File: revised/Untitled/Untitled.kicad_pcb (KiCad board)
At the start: 2 copper layers, 168 x 134.2 mm, 42 parts, among them J1 Conn_01x02_Pin, J2 USB_C_Receptacle_USB2.0_16P, J3 ARM Cortex Debug, J4 Conn_Coaxial, J5 Screw_Terminal_01x02, J6 Screw_Terminal_01x02, J7 Screw_Terminal_01x02, Q1 Q_PMOS, Q2 NMOS, Q3 NMOS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

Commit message: layout revised
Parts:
- J5, J7: footprint TerminalBlock:TerminalBlock_MaiXu_MX126-5.0-02P_1x02_P5.00mm -> TerminalBlock_Phoenix:TerminalBlock_Phoenix_MKDS-1,5-2-5.08_1x02_P5.08mm_Horizontal
- moved J7 153.1 mm to (123.7, 144.8)
- moved Q3 136.8 mm to (127.0, 135.5)
- moved R8 135.8 mm to (133.2, 134.2), turned to 90 degrees
- moved R9 134.8 mm to (131.5, 134.2), turned to 90 degrees
- moved C15 115.2 mm to (124.6, 171.0)
- moved C14 115.2 mm to (124.6, 168.5)
- moved J5 100.1 mm to (135.2, 145.2)
- moved D1 92.4 mm to (159.5, 118.9), turned to -90 degrees
- moved Q2 90.0 mm to (137.8, 137.5)
- moved R4 89.0 mm to (163.0, 120.7), turned to -90 degrees
- moved R5 88.5 mm to (166.2, 119.7)
- moved C5 86.0 mm to (159.2, 112.4), turned to 180 degrees
- moved U3 84.2 mm to (165.8, 110.2)
- moved C7 80.1 mm to (159.1, 110.2), turned to 180 degrees
- moved Q1 79.1 mm to (164.5, 116.7), turned to 180 degrees
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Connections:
- Q2 pad 1: Net-(J5-Pin_1) -> Net-(J5-Pin_2)
- Q2 pad 3: Net-(J5-Pin_2) -> Net-(J5-Pin_1)
- Q3 pad 1: Net-(J7-Pin_1) -> Net-(J7-Pin_2)
- Q3 pad 3: Net-(J7-Pin_2) -> Net-(J7-Pin_1)
- U2 pad 26: SWDIO -> RADIO_SCK
- U2 pad 27: SWCLK -> RADIO_MISO
- U2 pad 28: unconnected-(U2-PB15-Pad28) -> RADIO_MOSI
- U2 pad 34: RADIO_SCK -> SWDIO
- U2 pad 37: RADIO_MISO -> SWCLK
- U2 pad 38: RADIO_MOSI -> unconnected-(U2-PA15-Pad38)
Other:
- board size 168 x 134.2 mm -> 73.5 x 67.1 mm

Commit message: signal routing start
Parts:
- added H1: MountingHole_Pad, MountingHole:MountingHole_4.3mm_M4_DIN965_Pad_TopBottom, F.Cu at (161.5, 145.5)
- added H2: MountingHole_Pad, MountingHole:MountingHole_4.3mm_M4_DIN965_Pad_TopBottom, F.Cu at (105.0, 145.0)
- added H3: MountingHole_Pad, MountingHole:MountingHole_4.3mm_M4_DIN965_Pad_TopBottom, F.Cu at (105.0, 94.5)
- added H4: MountingHole_Pad, MountingHole:MountingHole_4.3mm_M4_DIN965_Pad_TopBottom, F.Cu at (161.5, 94.5)
- moved C1 24.4 mm to (154.8, 107.0), turned to 180 degrees
- moved U3 21.7 mm to (153.0, 127.8), turned to 180 degrees
- moved C4 21.7 mm to (151.5, 111.0), turned to -90 degrees
- moved C6 20.8 mm to (159.2, 128.8), turned to 0 degrees
- moved U1 18.1 mm to (154.8, 110.5), turned to 180 degrees
- moved R1 17.4 mm to (151.2, 139.5)
- moved C7 16.3 mm to (159.4, 126.5), turned to 0 degrees
- moved C2 16.0 mm to (158.0, 110.5), turned to 90 degrees
- moved C3 15.8 mm to (159.8, 110.5), turned to 90 degrees
- moved L1 13.6 mm to (154.8, 113.2), turned to 0 degrees
- moved C5 11.8 mm to (159.2, 124.2), turned to 0 degrees
- moved J6 10.0 mm to (152.5, 94.3)
- moved R2 9.75 mm to (155.0, 139.0), turned to 0 degrees
- moved R5 8.91 mm to (158.2, 115.8), turned to 180 degrees
- moved U6 8.76 mm to (146.1, 107.5)
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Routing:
- net USB_DETECT: track 0.00 -> 43.7 mm
- net +3.3V: track 0.00 -> 40.4 mm
- net USB5V: track 0.00 -> 32.8 mm
- net USB_DP: track 0.00 -> 30.0 mm
- net USB_DM: track 0.00 -> 28.8 mm
- net STM_TX_ETH_RX: track 0.00 -> 23.5 mm
- net STM_RX_ETH_TX: track 0.00 -> 23.1 mm
- net +8V: track 0.00 -> 22.3 mm
- net STM_TX_LORA_RX: track 0.00 -> 21.0 mm, vias 0 -> 2
- net STM_RX_LORA_TX: track 0.00 -> 20.2 mm, vias 0 -> 2
- net +5V: track 0.00 -> 17.2 mm
- net Net-(D1-K): track 0.00 -> 10.7 mm
- net Net-(Q1-G): track 0.00 -> 9.09 mm
- net SWDIO: track 0.00 -> 8.68 mm
- net Net-(U1-SW): track 0.00 -> 6.99 mm
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- added copper zone on F.Cu, net +3.3V
- added copper zone on F.Cu, net +8V
- added copper zone on B.Cu, net GND
- added copper zone on F.Cu, net GND
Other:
- board size 73.5 x 67.1 mm -> 66 x 60.1 mm

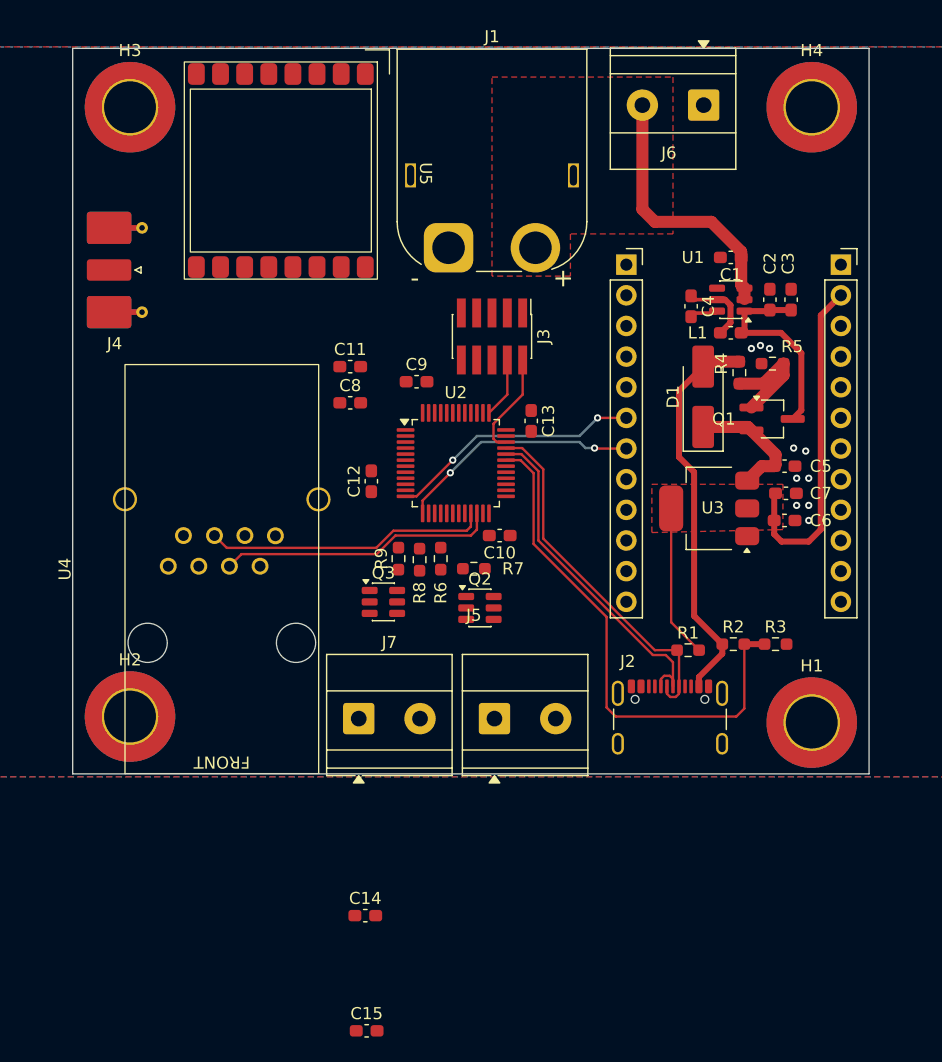
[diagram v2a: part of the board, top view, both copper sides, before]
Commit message: optocouplers added
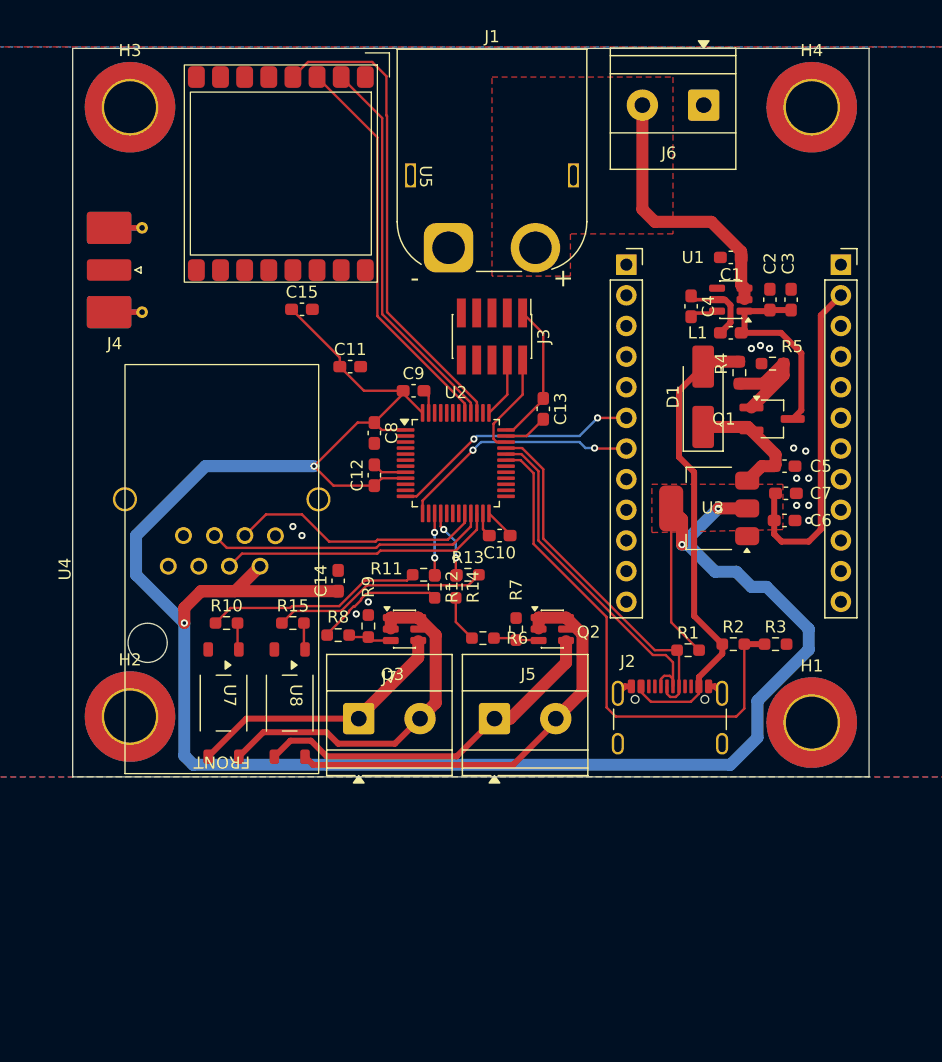
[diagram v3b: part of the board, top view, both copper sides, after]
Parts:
- added R10: 180, Resistor_SMD:R_0603_1608Metric_Pad0.98x0.95mm_HandSolder, F.Cu at (113.0, 137.2)
- added R11: 0, Resistor_SMD:R_0603_1608Metric_Pad0.98x0.95mm_HandSolder, F.Cu at (129.3, 133.2)
- added R12: 0, Resistor_SMD:R_0603_1608Metric_Pad0.98x0.95mm_HandSolder, F.Cu at (130.2, 134.2)
- added R13: 0, Resistor_SMD:R_0603_1608Metric_Pad0.98x0.95mm_HandSolder, F.Cu at (133.0, 133.2)
- added R14: 0, Resistor_SMD:R_0603_1608Metric_Pad0.98x0.95mm_HandSolder, F.Cu at (132.0, 134.2)
- added R15: 180, Resistor_SMD:R_0603_1608Metric_Pad0.98x0.95mm_HandSolder, F.Cu at (118.5, 137.2)
- added U7: opto, UCIRP-KiCAD-Lib:optocoupler, F.Cu at (112.8, 143.2)
- added U8: opto, UCIRP-KiCAD-Lib:optocoupler, F.Cu at (118.2, 143.2)
- moved C15 60.0 mm to (119.2, 111.2)
- moved C14 27.8 mm to (122.2, 133.8), turned to 90 degrees
- moved R8 9.20 mm to (122.2, 138.2), turned to 180 degrees
- moved R6 7.46 mm to (134.2, 138.5), turned to 180 degrees
- moved Q2 6.25 mm to (140.0, 137.8)
- moved R9 6.12 mm to (124.8, 137.5)
- moved R7 6.10 mm to (137.0, 137.8), turned to 90 degrees
- moved C8 3.20 mm to (125.2, 121.5), turned to -90 degrees
- moved Q3 2.85 mm to (127.8, 137.8)
- moved C13 1.41 mm to (139.2, 119.5)
- moved C9 0.79 mm to (128.5, 118.0)
- moved C12 0.56 mm to (125.2, 125.0)
- moved U5 0.25 mm to (117.5, 100.0)
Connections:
- net Net-(J5-Pin_2) renamed st12
- net Net-(J7-Pin_2) renamed st22
- J5 pad 1: Net-(J5-Pin_1) -> st11
- J7 pad 1: Net-(J7-Pin_1) -> st21
- Q2 pad 3: Net-(J5-Pin_1) -> Net-(Q2-G)
- Q2 pad 4: Net-(Q2-S) -> st11
- Q3 pad 3: Net-(J7-Pin_1) -> Net-(Q3-G)
- Q3 pad 4: Net-(Q3-S) -> st21
- R6 pad 1: Net-(Q2-S) -> Net-(Q2-G)
- R6 pad 2: NMOS1 -> Net-(R14-Pad2)
- R7 pad 1: Net-(Q2-S) -> Net-(Q2-G)
- R8 pad 1: Net-(Q3-S) -> Net-(Q3-G)
- R8 pad 2: NMOS2 -> Net-(R12-Pad2)
- R9 pad 1: Net-(Q3-S) -> Net-(Q3-G)
- U2 pad 26: RADIO_SCK -> unconnected-(U2-PB13-Pad26)
- U2 pad 27: RADIO_MISO -> unconnected-(U2-PB14-Pad27)
- U2 pad 28: RADIO_MOSI -> unconnected-(U2-PB15-Pad28)
- U2 pad 39: unconnected-(U2-PB3-Pad39) -> RADIO_SCK
- U2 pad 40: unconnected-(U2-PB4-Pad40) -> RADIO_MISO
- U2 pad 41: unconnected-(U2-PB5-Pad41) -> RADIO_MOSI
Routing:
- net +3.3V: track 40.4 -> 231.7 mm, vias 0 -> 4
- net RADIO_SCK: track 0.00 -> 39.8 mm
- net st12: track 0.00 -> 35.8 mm
- net RADIO_MOSI: track 0.00 -> 32.9 mm
- net RADIO_MISO: track 0.00 -> 32.3 mm
- net st11: track 0.00 -> 30.3 mm
- net st22: track 0.00 -> 29.8 mm
- net st21: track 0.00 -> 22.2 mm
- net ETH_RST: track 0.00 -> 21.3 mm
- net Net-(R10-Pad1): track 0.00 -> 18.0 mm
- net Net-(R13-Pad2): track 0.00 -> 18.0 mm
- net GND: track 0.00 -> 13.3 mm, vias 10 -> 14
- net Net-(R12-Pad2): track 0.00 -> 10.7 mm
- net USB5V: track 32.8 -> 39.3 mm
- net NMOS1: track 0.00 -> 5.36 mm, vias 0 -> 2
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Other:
- board size 66 x 60.1 mm -> 66 x 60.4 mm

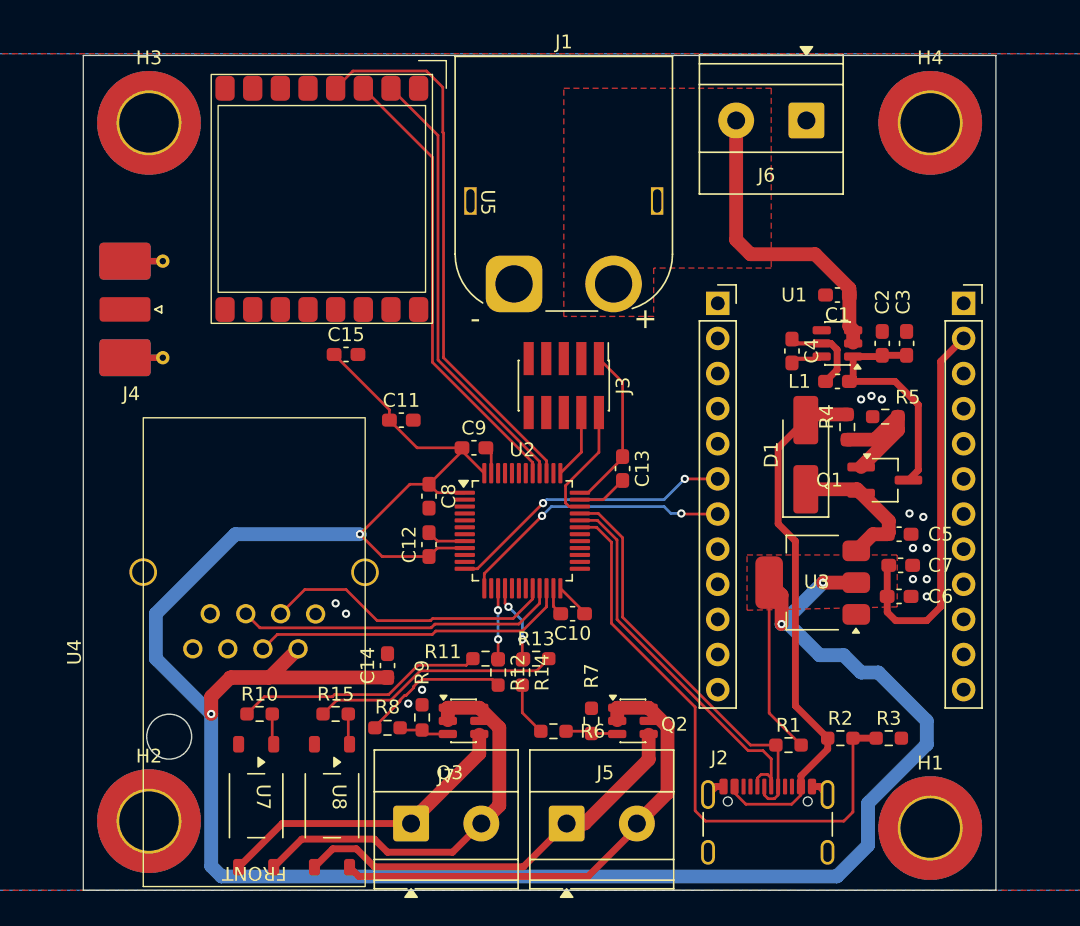
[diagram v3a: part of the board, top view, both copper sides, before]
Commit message: cleaned up layout and board shape finalized
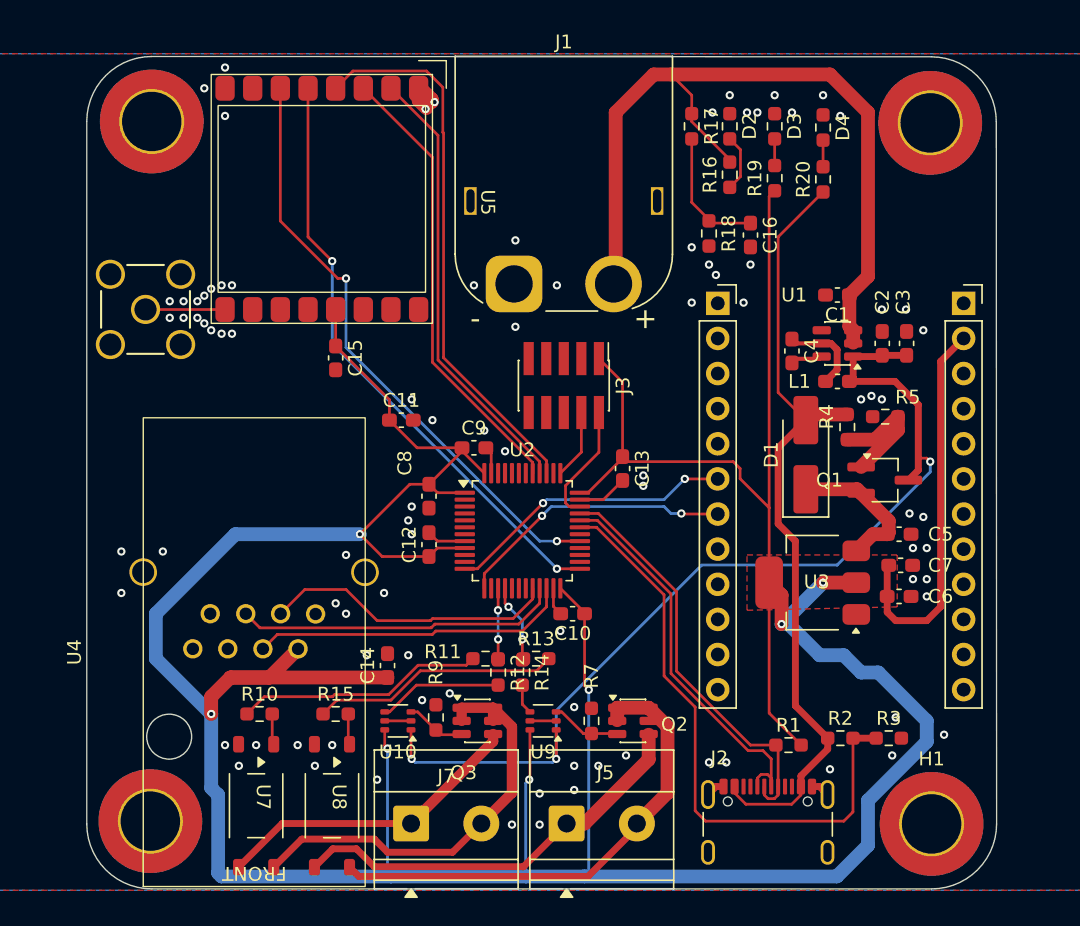
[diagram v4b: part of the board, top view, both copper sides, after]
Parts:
- removed J6: Screw_Terminal_01x02, TerminalBlock_Phoenix:TerminalBlock_Phoenix_MKDS-1,5-2-5.08_1x02_P5.08mm_Horizontal
- removed R6, R8: 100, Resistor_SMD:R_0603_1608Metric_Pad0.98x0.95mm_HandSolder
- added C16: 100nf, Capacitor_SMD:C_0603_1608Metric_Pad1.08x0.95mm_HandSolder, F.Cu at (148.5, 102.6)
- added D2: LED, Resistor_SMD:R_0603_1608Metric_Pad0.98x0.95mm_HandSolder, F.Cu at (147.0, 94.8)
- added D3: LED, Resistor_SMD:R_0603_1608Metric_Pad0.98x0.95mm_HandSolder, F.Cu at (150.2, 94.8)
- added D4: LED, Resistor_SMD:R_0603_1608Metric_Pad0.98x0.95mm_HandSolder, F.Cu at (153.8, 94.8)
- added R16: 560, Resistor_SMD:R_0603_1608Metric_Pad0.98x0.95mm_HandSolder, F.Cu at (147.0, 98.2)
- added R17: 10k, Resistor_SMD:R_0603_1608Metric_Pad0.98x0.95mm_HandSolder, F.Cu at (144.2, 94.8)
- added R18: 6.8k, Resistor_SMD:R_0603_1608Metric_Pad0.98x0.95mm_HandSolder, F.Cu at (145.5, 102.5)
- added R19: 150, Resistor_SMD:R_0603_1608Metric_Pad0.98x0.95mm_HandSolder, F.Cu at (150.2, 98.5)
- added R20: 330, Resistor_SMD:R_0603_1608Metric_Pad0.98x0.95mm_HandSolder, F.Cu at (153.8, 98.6)
- added U10: SN74LVC1T45DCK, Package_TO_SOT_SMD:SOT-363_SC-70-6, F.Cu at (123.0, 137.8)
- added U9: SN74LVC1T45DCK, Package_TO_SOT_SMD:SOT-363_SC-70-6, F.Cu at (133.5, 137.8)
- J4: footprint Connector_Coaxial:SMA_Molex_73251-2120_EdgeMount_Horizontal -> UCIRP-KiCAD-Lib:CONN_73391-0070_MOL
- moved J4 1.73 mm to (104.8, 108.0)
- moved Q3 1.00 mm to (128.8, 137.8)
- moved R9 1.00 mm to (125.8, 137.5)
- moved C15 0.79 mm to (118.5, 111.5), turned to -90 degrees
- moved H1 0.32 mm to (161.6, 145.2)
- moved H3 0.22 mm to (105.2, 94.4)
- moved H2 0.10 mm to (105.1, 145.0)
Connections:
- net Net-(Q2-G) renamed LOGICA1
- net Net-(Q3-G) renamed LOGICA2
- R12 pad 2: Net-(R12-Pad2) -> LOGICB2
- R14 pad 2: Net-(R14-Pad2) -> LOGICB1
- U2 pad 17: ETH_CTS -> unconnected-(U2-PA7-Pad17)
- U2 pad 18: ETH_DTR -> unconnected-(U2-PB0-Pad18)
- U2 pad 19: ETH_RTS -> unconnected-(U2-PB1-Pad19)
- U4 pad 6: ETH_RTS -> unconnected-(U4-CP1/RTS-Pad6)
- U4 pad 7: ETH_DTR -> unconnected-(U4-CP2/DTR-Pad7)
- U4 pad 8: ETH_CTS -> unconnected-(U4-CP3/CTS/DCD-Pad8)
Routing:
- net +3.3V: track 231.7 -> 316.8 mm, vias 4 -> 7
- net +5V: track 17.2 -> 71.5 mm, vias 0 -> 3
- net RADIO_CS: track 0.00 -> 43.9 mm, vias 0 -> 2
- net RADIO_nRST: track 0.00 -> 43.8 mm, vias 0 -> 2
- net +8V: track 22.3 -> 58.4 mm
- net USB5V: track 39.3 -> 57.9 mm
- net Net-(R12-Pad2): track 10.7 -> 0.00 mm
- net ADC1: track 0.00 -> 9.51 mm
- net LOGICB2: track 0.00 -> 9.00 mm
- net GND: track 13.3 -> 20.2 mm, vias 14 -> 92
- net Net-(J4-In): track 0.00 -> 6.25 mm
- net Net-(D2-A): track 0.00 -> 4.14 mm
- net Net-(R14-Pad2): track 3.89 -> 0.00 mm
- net LOGICB1: track 0.00 -> 2.17 mm
- net Net-(D4-A): track 0.00 -> 1.93 mm
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- removed copper zone on F.Cu, net +8V
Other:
- board size 66 x 60.4 mm -> 65.8 x 60.2 mm

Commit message: prereview board
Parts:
- added Y1: 16MHz, Crystal:Crystal_SMD_2016-4Pin_2.0x1.6mm, F.Cu at (124.9, 120.2)
- moved C8 3.25 mm to (122.1, 122.3)
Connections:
- U2 pad 44: unconnected-(U2-BOOT0-Pad44) -> GND
- U2 pad 5: unconnected-(U2-PD0-Pad5) -> Net-(U2-PD0)
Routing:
- net Net-(U2-PD0): track 0.00 -> 3.79 mm
- net +3.3V: track 316.8 -> 318.3 mm
